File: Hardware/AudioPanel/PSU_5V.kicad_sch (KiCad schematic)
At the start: 16 parts, among them U63 LM1084-ADJ, U64 NE5534

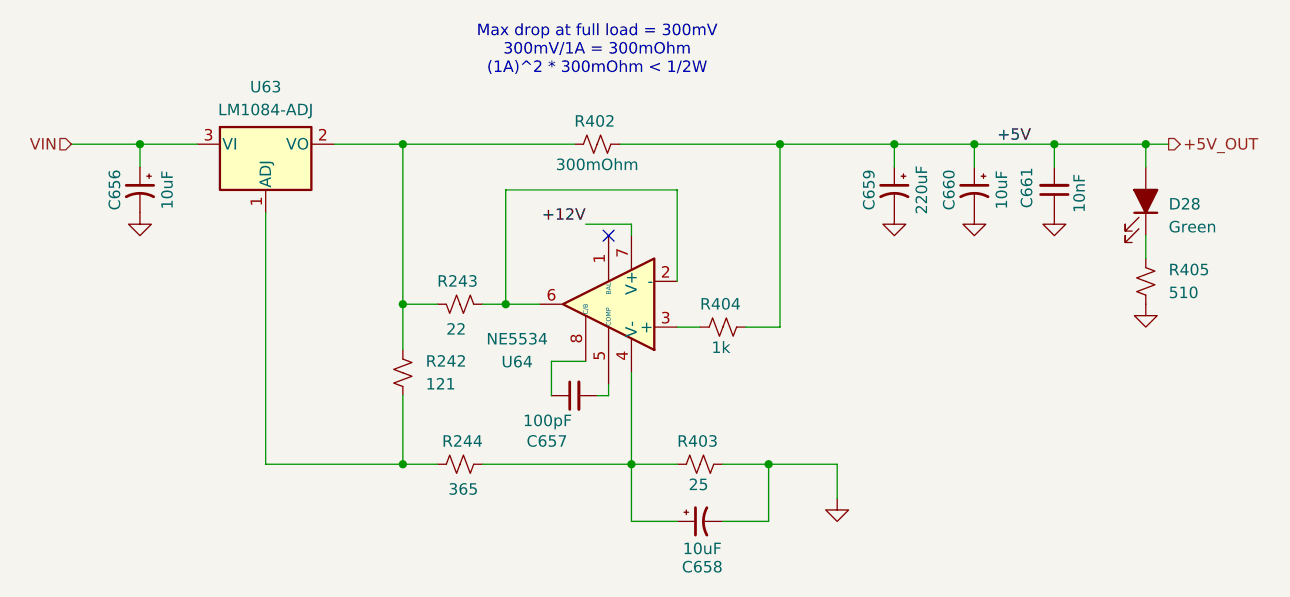
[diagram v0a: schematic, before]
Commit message: Realized that I need to rethink how I'm going to mix the radio audio with the stereo audio
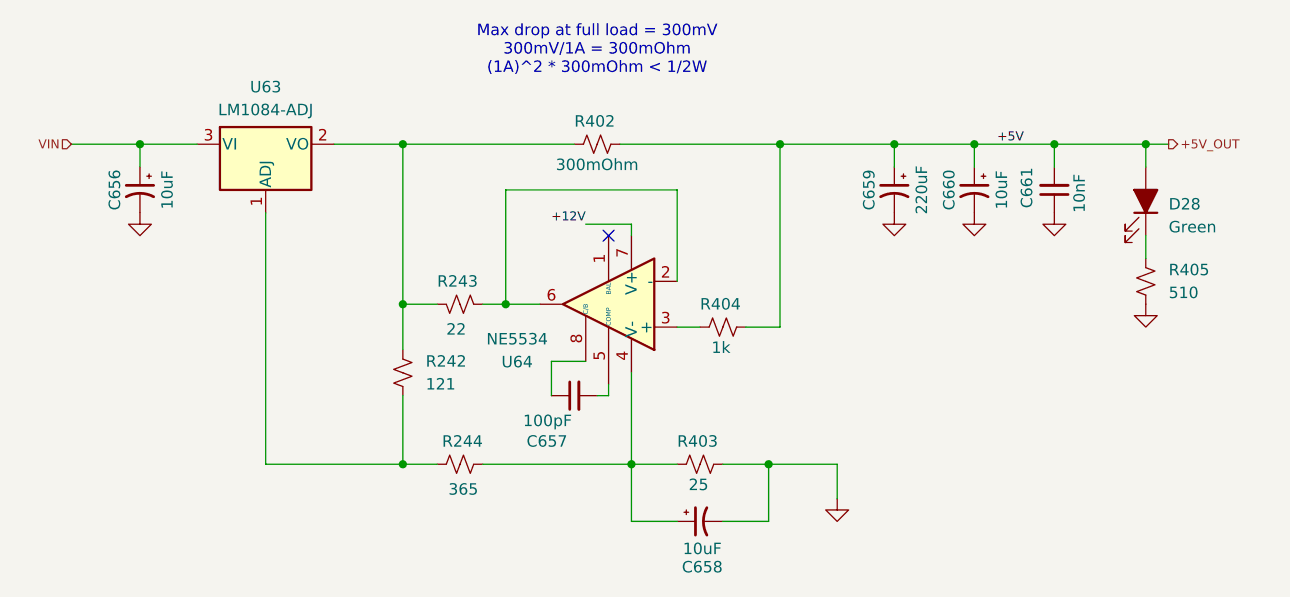
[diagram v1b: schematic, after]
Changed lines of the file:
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@@
 		(effects
 			(font
-				(size 1.27 1.27)
+				(size 1 1)
 			)
 			(justify right bottom)
@@
 		(effects
 			(font
-				(size 1.27 1.27)
+				(size 1 1)
 			)
 			(justify left bottom)
@@
 		(effects
 			(font
-				(size 1.27 1.27)
+				(size 1 1)
 			)
 			(justify right)
@@
 		(effects
 			(font
-				(size 1.27 1.27)
+				(size 1 1)
 			)
 			(justify left)
